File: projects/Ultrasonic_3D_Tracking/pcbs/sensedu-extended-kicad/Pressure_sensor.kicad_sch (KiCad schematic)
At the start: 6 parts, among them J18 Conn_03x01, U8 DPS310XTSA1

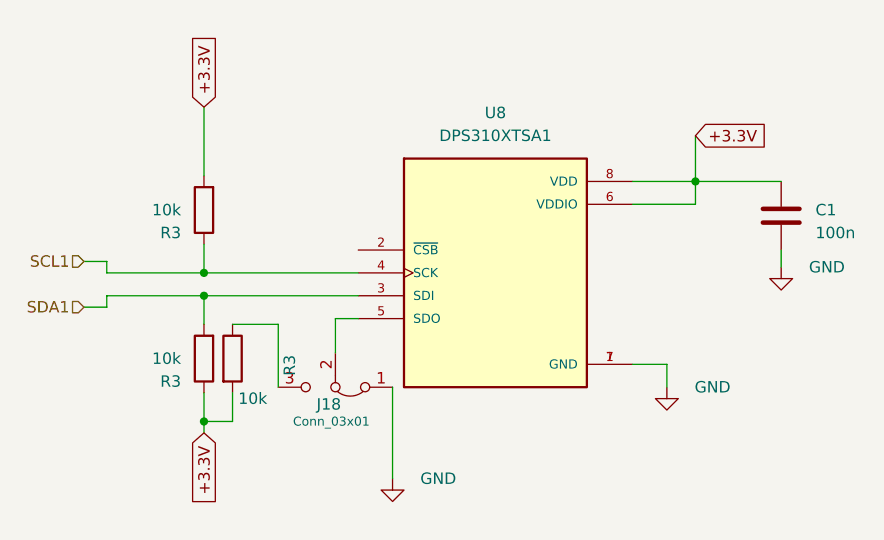
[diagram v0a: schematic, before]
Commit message: Fix: Cleaned schematic
- project is not correctly set up, so cannot be ordered without further
   work
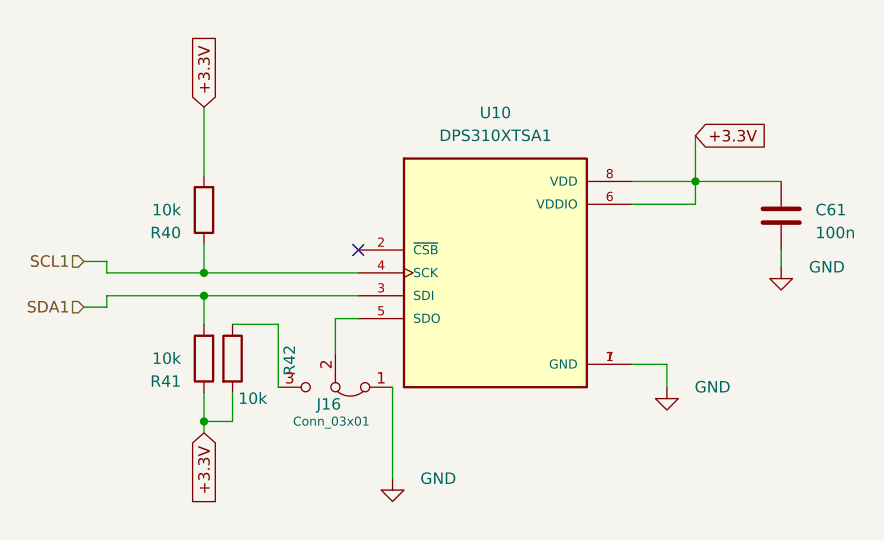
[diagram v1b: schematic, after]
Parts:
- renumbered C1 to C61, J18 to J16, R3 to R40, R3 to R41, R3 to R42, U8 to U10
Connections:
- no-connect marks 0 -> 1
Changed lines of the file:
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@@
 		(color 0 0 0 0)
+	)
+	(no_connect
+		(at 118.11 82.55)
 	)
 	(wire
@@
 		(dnp no)
 		(fields_autoplaced yes)
-		(property "Reference" "U8"
+		(property "Reference" "U10"
 			(at 133.35 67.31 0)
 			(effects
@@
 		)
 		(pin "5"
+		)
+		(instances
+			(project "Ultrasound shield_8mic"
+				(path "/e63e39d7-6ac0-4ffd-8aa3-1841a4541b55/d6e506e4-1660-4f12-9b07-0782300f1012"
+					(reference "U10")
+					(unit 1)
+				)
+			)
 		)
 	)
@@
 		(on_board yes)
 		(dnp no)
-		(property "Reference" "#PWR07"
+		(property "Reference" "#PWR055"
 			(at 165.1 90.805 0)
 			(effects
@@
 		)
 		(pin "1"
+		)
+		(instances
+			(project "Ultrasound shield_8mic"
+				(path "/e63e39d7-6ac0-4ffd-8aa3-1841a4541b55/d6e506e4-1660-4f12-9b07-0782300f1012"
+					(reference "#PWR055")
+					(unit 1)
+				)
+			)
 		)
 	)
@@
 		(on_board yes)
 		(dnp no)
-		(property "Reference" "#PWR07"
+		(property "Reference" "#PWR056"
 			(at 152.4 104.14 0)
 			(effects
@@
 		)
 		(pin "1"
+		)
+		(instances
+			(project "Ultrasound shield_8mic"
+				(path "/e63e39d7-6ac0-4ffd-8aa3-1841a4541b55/d6e506e4-1660-4f12-9b07-0782300f1012"
+					(reference "#PWR056")
+					(unit 1)
+				)
+			)
 		)
 	)
@@
 		(on_board yes)
 		(dnp no)
-		(property "Reference" "R3"
+		(property "Reference" "R41"
 			(at 98.425 97.155 0)
 			(effects
@@
 		)
 		(pin "2"
+		)
+		(instances
+			(project "Ultrasound shield_8mic"
+				(path "/e63e39d7-6ac0-4ffd-8aa3-1841a4541b55/d6e506e4-1660-4f12-9b07-0782300f1012"
+					(reference "R41")
+					(unit 1)
+				)
+			)
 		)
 	)
@@
 		(dnp no)
 		(fields_autoplaced yes)
-		(property "Reference" "C1"
+		(property "Reference" "C61"
 			(at 168.91 78.105 0)
 			(effects
@@
 		)
 		(pin "2"
+		)
+		(instances
+			(project "Ultrasound shield_8mic"
+				(path "/e63e39d7-6ac0-4ffd-8aa3-1841a4541b55/d6e506e4-1660-4f12-9b07-0782300f1012"
+					(reference "C61")
+					(unit 1)
+				)
+			)
 		)
 	)
@@
 		(on_board yes)
 		(dnp no)
-		(property "Reference" "R3"
+		(property "Reference" "R40"
 			(at 98.425 80.645 0)
 			(effects
@@
 		)
 		(pin "2"
+		)
+		(instances
+			(project "Ultrasound shield_8mic"
+				(path "/e63e39d7-6ac0-4ffd-8aa3-1841a4541b55/d6e506e4-1660-4f12-9b07-0782300f1012"
+					(reference "R40")
+					(unit 1)
+				)
+			)
 		)
 	)
@@
 		(on_board yes)
 		(dnp no)
-		(property "Reference" "J18"
+		(property "Reference" "J16"
 			(at 116.205 99.695 0)
 			(effects
@@
 		)
 		(pin "3"
+		)
+		(instances
+			(project "Ultrasound shield_8mic"
+				(path "/e63e39d7-6ac0-4ffd-8aa3-1841a4541b55/d6e506e4-1660-4f12-9b07-0782300f1012"
+					(reference "J16")
+					(unit 1)
+				)
+			)
 		)
 	)
@@
 		(on_board yes)
 		(dnp no)
-		(property "Reference" "R3"
+		(property "Reference" "R42"
 			(at 110.49 96.52 90)
 			(effects
@@
 		)
 		(pin "2"
+		)
+		(instances
+			(project "Ultrasound shield_8mic"
+				(path "/e63e39d7-6ac0-4ffd-8aa3-1841a4541b55/d6e506e4-1660-4f12-9b07-0782300f1012"
+					(reference "R42")
+					(unit 1)
+				)
+			)
 		)
 	)
@@
 		(on_board yes)
 		(dnp no)
-		(property "Reference" "#PWR07"
+		(property "Reference" "#PWR057"
 			(at 121.92 114.3 0)
 			(effects
@@
 		(pin "1"
 		)
-	)
+		(instances
+			(project "Ultrasound shield_8mic"
+				(path "/e63e39d7-6ac0-4ffd-8aa3-1841a4541b55/d6e506e4-1660-4f12-9b07-0782300f1012"
+					(reference "#PWR057")
+					(unit 1)
+				)
+			)
+		)
+	)
